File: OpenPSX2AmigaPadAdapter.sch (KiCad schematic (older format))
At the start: 44 parts, among them J1 TO_PSX_PAD, J2 DB9_F, J3 CONN_FTDI, J4 CONN_ICSP, J99 OSHW_LOGO, Q1 BSS138, Q2 BSS138, Q3 BSS138, Q4 BSS138, Q5 BSS138, SW1 RESET, U1 ATmega328P-AU, U2 LM1117-3.3, Y1 16M, Y2 16M

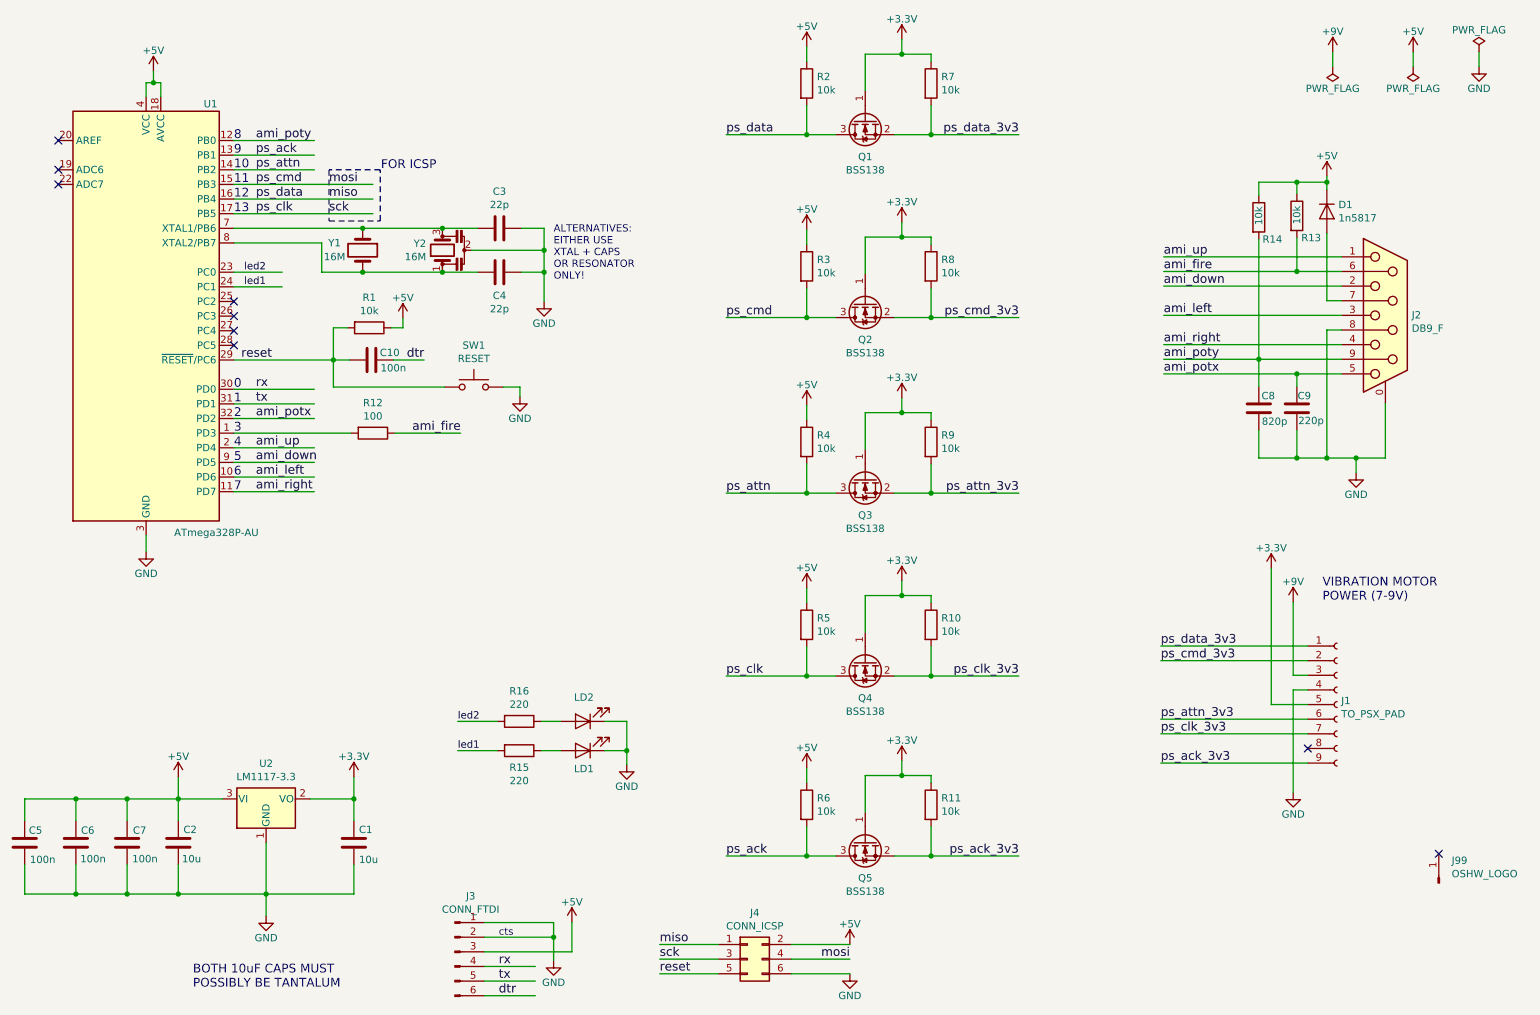
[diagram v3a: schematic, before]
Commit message: Fix component naming
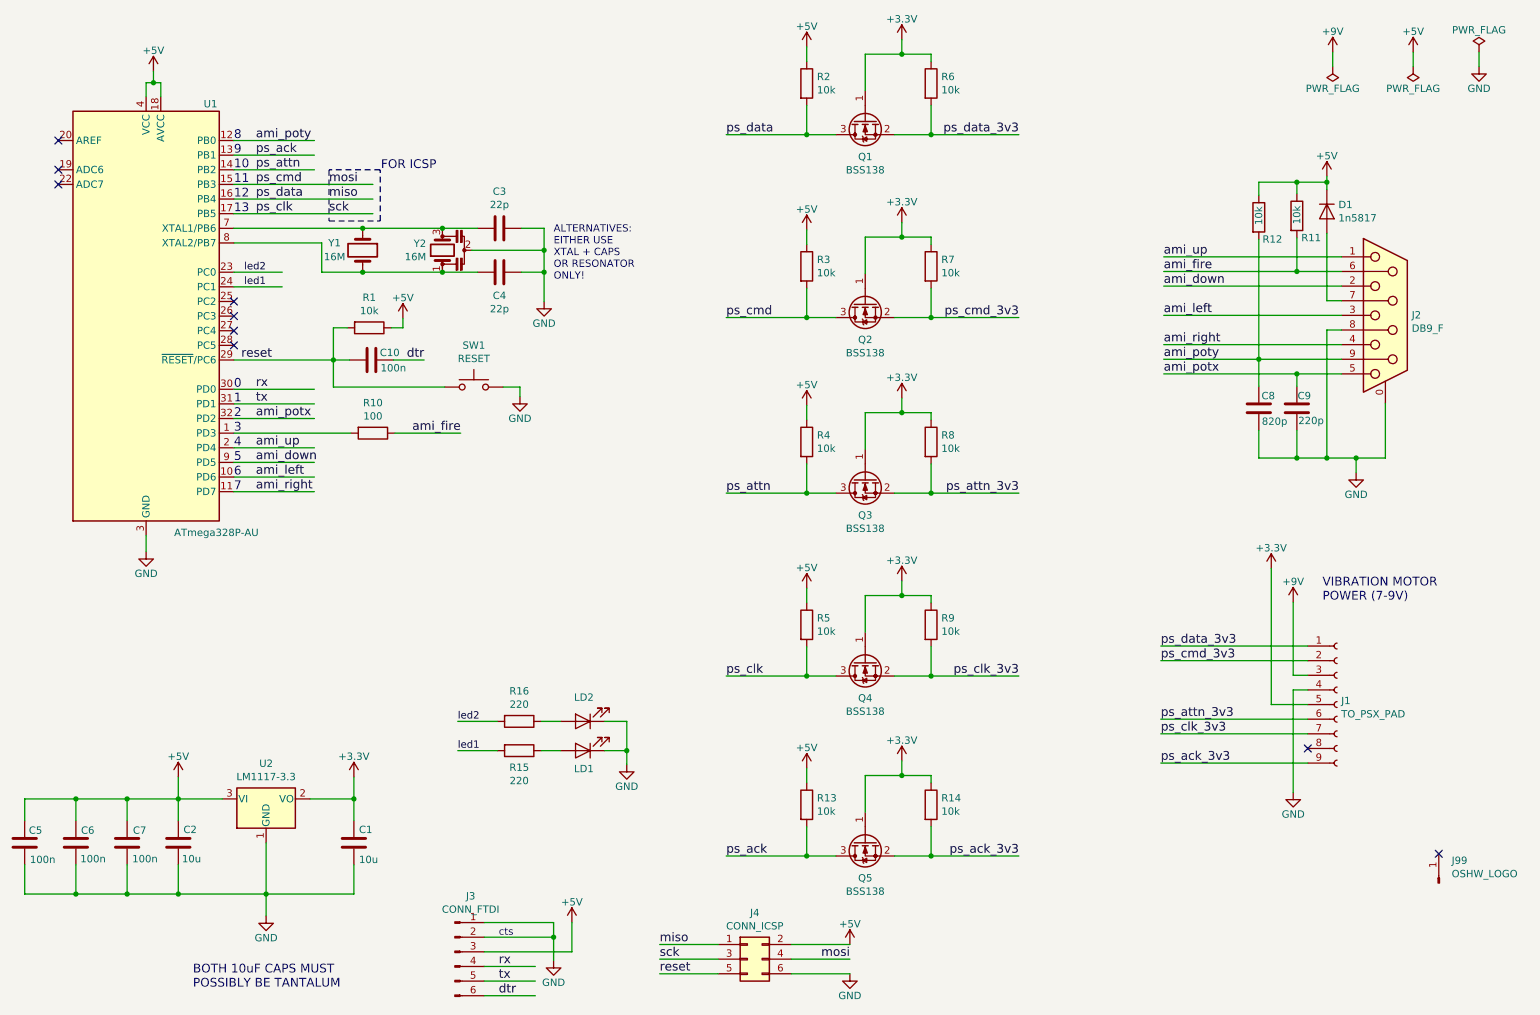
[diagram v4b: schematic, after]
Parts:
- renumbered R12 to R10, R13 to R11, R14 to R12, R6 to R13, R11 to R14, R7 to R6, R8 to R7, R9 to R8, R10 to R9
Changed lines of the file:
@@
 Sheet 1 1
 Title "OpenPSX2AmigaPadAdapter"
-Date "2019-12-10"
+Date "2020-01-02"
 Rev "3"
 Comp "SukkoPera"
@@
 $EndComp
 $Comp
-L Device:R R7
+L Device:R R6
 U 1 1 5D1E6A38
 P 7155 1015
-F 0 "R7" H 7225 1061 50  0000 L CNN
+F 0 "R6" H 7225 1061 50  0000 L CNN
 F 1 "10k" H 7225 970 50  0000 L CNN
 F 2 "Resistor_SMD:R_0805_2012Metric_Pad1.15x1.40mm_HandSolder" V 7085 1015 50  0001 C CNN
@@
 $EndComp
 $Comp
-L Device:R R8
+L Device:R R7
 U 1 1 5D1F51C8
 P 7155 2265
-F 0 "R8" H 7225 2311 50  0000 L CNN
+F 0 "R7" H 7225 2311 50  0000 L CNN
 F 1 "10k" H 7225 2220 50  0000 L CNN
 F 2 "Resistor_SMD:R_0805_2012Metric_Pad1.15x1.40mm_HandSolder" V 7085 2265 50  0001 C CNN
@@
 $EndComp
 $Comp
-L Device:R R9
+L Device:R R8
 U 1 1 5D20380C
 P 7155 3465
-F 0 "R9" H 7225 3511 50  0000 L CNN
+F 0 "R8" H 7225 3511 50  0000 L CNN
 F 1 "10k" H 7225 3420 50  0000 L CNN
 F 2 "Resistor_SMD:R_0805_2012Metric_Pad1.15x1.40mm_HandSolder" V 7085 3465 50  0001 C CNN
@@
 $EndComp
 $Comp
-L Device:R R10
+L Device:R R9
 U 1 1 5D212533
 P 7155 4715
-F 0 "R10" H 7225 4761 50  0000 L CNN
+F 0 "R9" H 7225 4761 50  0000 L CNN
 F 1 "10k" H 7225 4670 50  0000 L CNN
 F 2 "Resistor_SMD:R_0805_2012Metric_Pad1.15x1.40mm_HandSolder" V 7085 4715 50  0001 C CNN
@@
 	6305 6295 6505 6295
 $Comp
-L Device:R R6
+L Device:R R13
 U 1 1 5DFD8E76
 P 6305 5945
-F 0 "R6" H 6375 5991 50  0000 L CNN
+F 0 "R13" H 6375 5991 50  0000 L CNN
 F 1 "10k" H 6375 5900 50  0000 L CNN
 F 2 "Resistor_SMD:R_0805_2012Metric_Pad1.15x1.40mm_HandSolder" V 6235 5945 50  0001 C CNN
@@
 $EndComp
 $Comp
-L Device:R R11
+L Device:R R14
 U 1 1 5DFD8E80
 P 7155 5945
-F 0 "R11" H 7225 5991 50  0000 L CNN
+F 0 "R14" H 7225 5991 50  0000 L CNN
 F 1 "10k" H 7225 5900 50  0000 L CNN
 F 2 "Resistor_SMD:R_0805_2012Metric_Pad1.15x1.40mm_HandSolder" V 7085 5945 50  0001 C CNN
@@
 ps_ack
 $Comp
-L Device:R R12
+L Device:R R10
 U 1 1 5D1D6EF3
 P 3340 3405
-F 0 "R12" V 3133 3405 50  0000 C CNN
+F 0 "R10" V 3133 3405 50  0000 C CNN
 F 1 "100" V 3224 3405 50  0000 C CNN
 F 2 "Resistor_SMD:R_0805_2012Metric_Pad1.15x1.40mm_HandSolder" V 3270 3405 50  0001 C CNN
@@
 $EndComp
 $Comp
-L Device:R R14
+L Device:R R12
 U 1 1 5DAFD7E8
 P 9395 1930
-F 0 "R14" H 9555 1780 50  0000 R CNN
+F 0 "R12" H 9555 1780 50  0000 R CNN
 F 1 "10k" V 9395 2005 50  0000 R CNN
 F 2 "Resistor_SMD:R_0805_2012Metric_Pad1.15x1.40mm_HandSolder" V 9325 1930 50  0001 C CNN
@@
 $EndComp
 $Comp
-L Device:R R13
+L Device:R R11
 U 1 1 5DAF3262
 P 9655 1920
-F 0 "R13" H 9820 1770 50  0000 R CNN
+F 0 "R11" H 9820 1770 50  0000 R CNN
 F 1 "10k" V 9655 1990 50  0000 R CNN
 F 2 "Resistor_SMD:R_0805_2012Metric_Pad1.15x1.40mm_HandSolder" V 9585 1920 50  0001 C CNN
